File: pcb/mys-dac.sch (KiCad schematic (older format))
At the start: 31 parts, among them J1 OLED, J2 Conn_02x20_Odd_Even, J3 Conn_02x20_Odd_Even, J4 DAC, J5 IO, J6 CONSOLE, U1 WM8805, U2 AP1117-ADJ, U3 ISO7321C, Y1 Crystal

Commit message: Almost completely routed
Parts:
- removed J?: Conn_02x03_Odd_Even, symbol Connector_Generic:Conn_02x03_Odd_Even
- removed U2: AP1117-ADJ, Package_TO_SOT_SMD:SOT-223-3_TabPin2, symbol Regulator_Linear:AP1117-ADJ
- added D1: SS14-E3/61T, Diode_SMD:D_SMA_Handsoldering, symbol Device:D_Schottky
- added F1: 2A, Fuse:Fuse_1812_4532Metric_Pad1.30x3.40mm_HandSolder, symbol Device:Polyfuse
- added H1, H2, H3, H4: MountingHole_Pad, MountingHole:MountingHole_2.5mm_Pad, symbol Mechanical:MountingHole_Pad
- added J7: SPDIF, micro-match:TE_MICRO-MATCH_FOB.14P, symbol Connector_Generic:Conn_02x07_Odd_Even
- added J8: PWR_IN, Connector_JST:JST_XH_B2B-XH-A_1x02_P2.50mm_Vertical, symbol Connector_Generic:Conn_01x02
- added L1: 2.2µ, Inductor_SMD:L_Taiyo-Yuden_NR-50xx_HandSoldering, symbol Device:L
- added U2: TLV62568DBV, Package_TO_SOT_SMD:SOT-23-5, symbol Regulator_Switching:TLV62568DBV
- C1: value C -> 22µ; footprint Capacitor_SMD:C_0805_2012Metric_Pad1.15x1.40mm_HandSolder -> Capacitor_SMD:C_1206_3216Metric_Pad1.42x1.75mm_HandSolder
- C2: value C -> 4.7µ; footprint Capacitor_SMD:C_0805_2012Metric_Pad1.15x1.40mm_HandSolder -> Capacitor_SMD:C_1206_3216Metric_Pad1.42x1.75mm_HandSolder
- C3, C5: value C -> 15p
- FB1: renamed from FB?; footprint (none) -> Inductor_SMD:L_0805_2012Metric_Pad1.15x1.40mm_HandSolder
- R2: value R -> 536k; DNP DNP -> (none)
- R3: value R -> 100k; DNP DNP -> (none)
- R4, R5: value R -> 4.7k
- Y1: value Crystal -> 12MHz
- gave numbers to parts that had none: 2
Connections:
- net VDD is gone; now on net +3V3: R4.1, R5.1, R6.1, R9.1
- net +3.8V: now also L1.2
- net +3V3: now also J4.2 (Pin_2), J5.2 (Pin_2), J7.2 (Pin_2)
- net +5V: now also F1.1, U2.1 (EN), U2.4 (VIN)
- net ENC1: now also J5.10 (Pin_10); no longer J5.14 (Pin_14)
- net ENC2: now also J5.11 (Pin_11); no longer J5.13 (Pin_13)
- net GND: now also C1.2, J4.1 (Pin_1), J5.1 (Pin_1), R10.2, H1.1, H2.1, H3.1, H4.1, J7.1 (Pin_1), J7.3 (Pin_3), J8.1 (Pin_1), U2.2 (GND); no longer R10.1
- net IMX_SPDIF_IN: now also J7.13 (Pin_13)
- net IMX_SPDIF_OUT: now also J7.14 (Pin_14)
- net IR: now also J5.15 (Pin_15); no longer J5.10 (Pin_10)
- net KPP_COL4: now also J5.8 (Pin_8); no longer J5.6 (Pin_6)
- net KPP_COL5: now also J5.3 (Pin_3); no longer J5.1 (Pin_1)
- net KPP_COL6: now also J5.5 (Pin_5); no longer J5.3 (Pin_3)
- net KPP_COL7: now also J5.9 (Pin_9); no longer J5.7 (Pin_7)
- net KPP_ROW4: now also J5.7 (Pin_7); no longer J5.5 (Pin_5)
- net KPP_ROW6: now also J5.4 (Pin_4); no longer J5.2 (Pin_2)
- net KPP_ROW7: now also J5.6 (Pin_6); no longer J5.4 (Pin_4)
- net PWM5_OUT: now also J5.14 (Pin_14); no longer J5.9 (Pin_9)
- net PWM8_OUT: now also J5.13 (Pin_13); no longer J5.11 (Pin_11)
- net SNVS_TAMPER8: now reaches J2.38 (Pin_38)
- net SNVS_TAMPER8: now also J5.16 (Pin_16)
- net PVDD: now reaches C9.1, FB1.1, U1.11 (PVDD)
- net at U1.2 (RX1): now also J7.4 (Pin_4)
- net at U1.21 (TX0): now also J7.12 (Pin_12)
- net at U1.22 (RX7/GPO6): now also J7.11 (Pin_11)
- net at U1.23 (RX6/GPO5): now also J7.10 (Pin_10)
- net at U1.24 (RX5/GPO4): now also J7.9 (Pin_9)
- net at U1.25 (RX4/GPO3): now also J7.8 (Pin_8)
- net at U1.26 (RX3): now also J7.7 (Pin_7)
- net at U1.27 (RX2): now also J7.6 (Pin_6)
- net at U1.3 (RX0): now also J7.5 (Pin_5)
- net at R9.2, U1.9 (~CSB~/GPO2): now also R10.1; no longer R10.2
- net at R2.2, R3.1: now also U2.5 (FB); no longer C1.2
- net IMX_ONOFF: no longer names the net of J2.32 (Pin_32)
- net IMX_POR: no longer names the net of J2.34 (Pin_34)
- net KPP_ROW5: no longer names the net of J3.18 (Pin_18)
- net KPP_ROW5: no longer J5.8 (Pin_8)
- new net: L1.1, U2.3 (SW)
- new net: D1.1 (K), F1.2
- new net: D1.2 (A), J8.2 (Pin_2)
- no-connect marks 13 -> 17
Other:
- note added: "I2C address\n0x3A (0x3B)"
- note added: "MYS-6ULX\nconnection"
- note added: "OLED"
- note added: "UART console isolation"
- note removed: "I2C address\n0x3A / 0x3B"
- moved on the sheet: C3, C4, C5, C6, C7, C8, C9, FB1, J1, J4, J5, J6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

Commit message: Done routing
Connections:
- net IR renamed IR_IN
- net PWM5_OUT renamed RED_LED
- net PWM7_OUT renamed GREEN_LED
- net PWM8_OUT renamed IR_OUT
- net SNVS_TAMPER8 renamed PWR_BTN
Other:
- note added: "DAC connection"
- note added: "ECSPI3_MISO"
- note added: "ECSPI3_MOSI"
- note added: "ECSPI3_SCLK"
- note added: "ECSPI3_SS0"
- note added: "Front panel\nconnection"
- note added: "GPIO1_IO18"
- note added: "GPIO1_IO24"
- note added: "GPIO1_IO25"
- note added: "GPIO1_IO26"
- note added: "GPIO1_IO27"
- note added: "GPIO1_IO28"
- note added: "GPIO1_IO29"
- note added: "GPIO4_IO14"
- note added: "GPIO4_IO17"
- note added: "GPIO4_IO18"
- note added: "GPIO4_IO25"
- note added: "GPIO5_IO08"
- note added: "I2C2_SCL"
- note added: "I2C2_SDA"
- note added: "KPP_COL04"
- note added: "KPP_COL05"
- note added: "KPP_COL06"
- note added: "KPP_COL07"
- note added: "KPP_ROW04"
- note added: "KPP_ROW06"
- note added: "KPP_ROW07"
- note added: "PWM5_OUT"
- note added: "PWM7_OUT"
- note added: "PWM8_OUT"
- note added: "Power input"
- note added: "S/PDIF multiplexer"
- note added: "SAI1_MCLK"
- note added: "SAI1_RX_BCLK"
- note added: "SAI1_RX_DATA"
- note added: "SAI1_RX_SYNC"
- note added: "SAI1_TX_DATA"
- note added: "SAI2_MCLK"
- note added: "SAI2_RX_DATA"
- note added: "SAI2_TX_BCLK"
- note added: "SAI2_TX_DATA"
- note added: "SAI2_TX_SYNC"
- note added: "SPDIF_IN"
- note added: "SPDIF_OUT"
- note added: "UART1_RX_DATA"
- note added: "UART1_TX_DATA"
- moved on the sheet: C1, C2, C3, C4, C5, C6, C7, C8, C9, D1, F1, FB1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

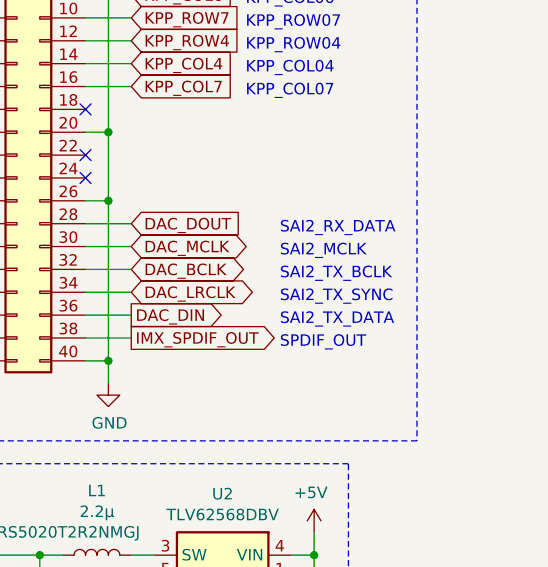
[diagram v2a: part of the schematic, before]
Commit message: Audio playback via WM8731 functional
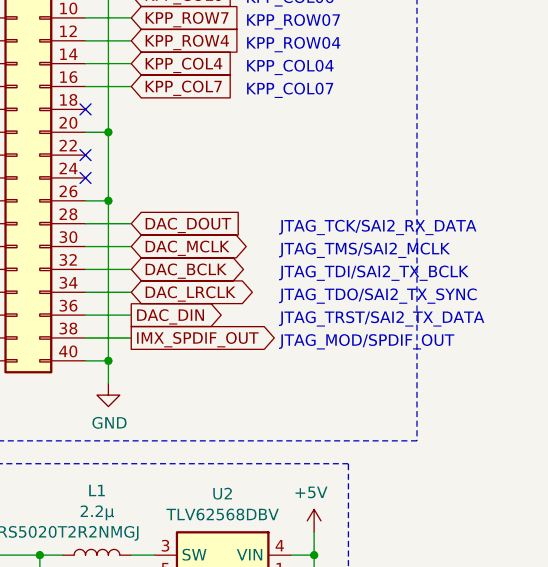
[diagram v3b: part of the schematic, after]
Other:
- note added: "JTAG_MOD/SPDIF_OUT"
- note added: "JTAG_TCK/SAI2_RX_DATA"
- note added: "JTAG_TDI/SAI2_TX_BCLK"
- note added: "JTAG_TDO/SAI2_TX_SYNC"
- note added: "JTAG_TMS/SAI2_MCLK"
- note added: "JTAG_TRST/SAI2_TX_DATA"
- note removed: "SAI2_MCLK"
- note removed: "SAI2_RX_DATA"
- note removed: "SAI2_TX_BCLK"
- note removed: "SAI2_TX_DATA"
- note removed: "SAI2_TX_SYNC"
- note removed: "SPDIF_OUT"
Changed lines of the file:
@@
 KPP_COL07
 Text Notes 6650 2350 0    50   ~ 0
-SAI2_RX_DATA
+JTAG_TCK/SAI2_RX_DATA
 Text Notes 6650 2750 0    50   ~ 0
-SAI2_TX_DATA
+JTAG_TRST/SAI2_TX_DATA
 Text Notes 6650 2550 0    50   ~ 0
-SAI2_TX_BCLK
+JTAG_TDI/SAI2_TX_BCLK
 Text Notes 6650 2650 0    50   ~ 0
-SAI2_TX_SYNC
+JTAG_TDO/SAI2_TX_SYNC
 Text Notes 6650 2450 0    50   ~ 0
-SAI2_MCLK
+JTAG_TMS/SAI2_MCLK
 Text Notes 6650 2850 0    50   ~ 0
-SPDIF_OUT
+JTAG_MOD/SPDIF_OUT
 Text Notes 3000 1550 0    50   ~ 0
 I2C2_SDA
